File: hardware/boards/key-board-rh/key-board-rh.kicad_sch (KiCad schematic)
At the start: 6 parts, among them J1 12-way, J2 2x12 1.27mm shrouded box head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, J3 1x10 2.54mm header pins, J4 1x10 2.54mm header pins, J5 4 wire pads

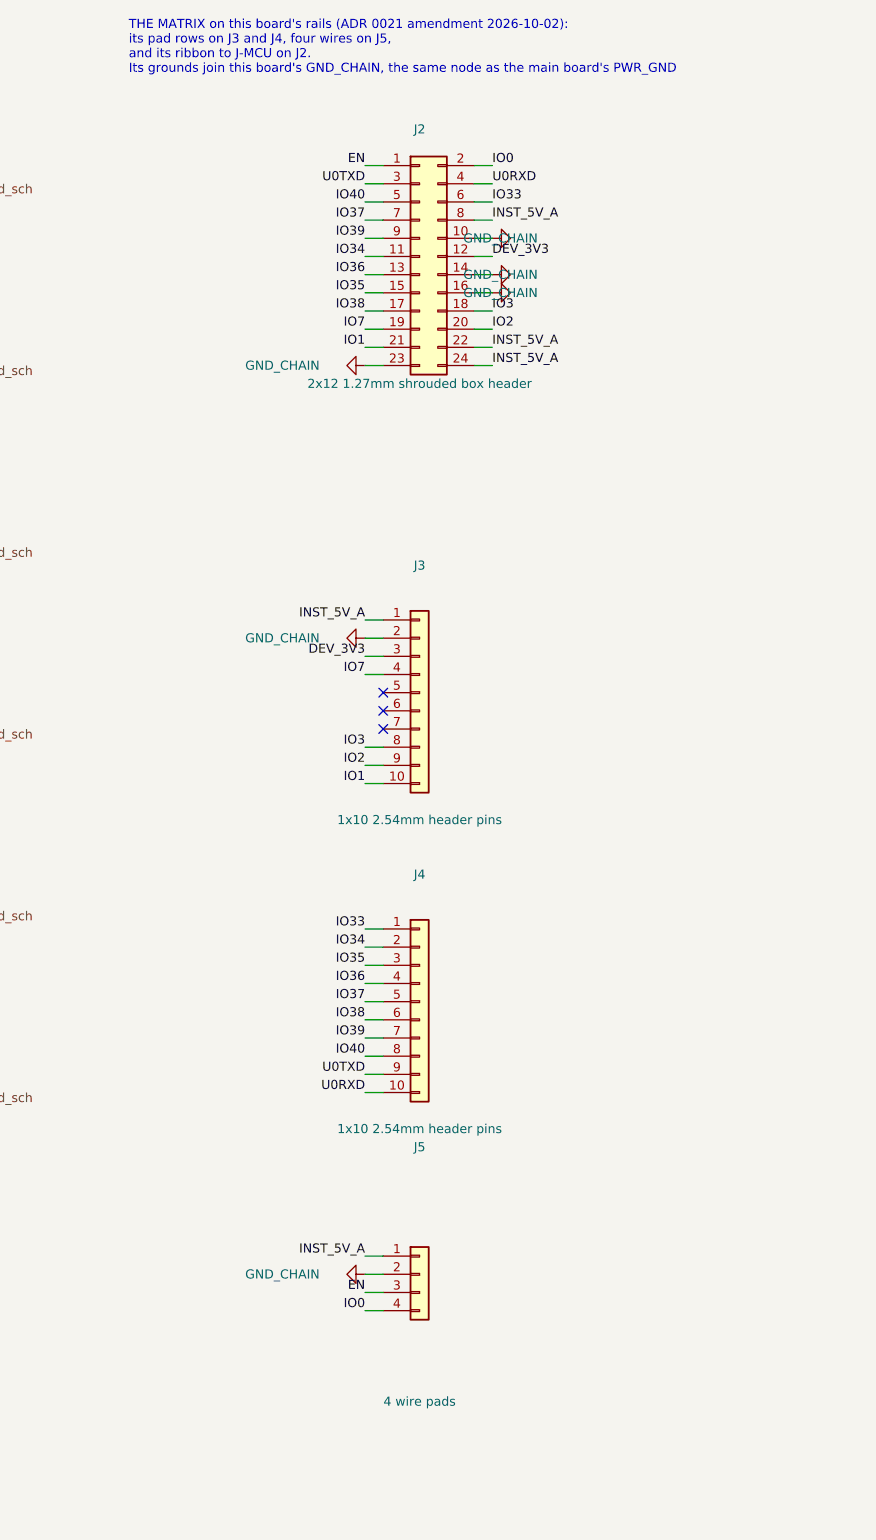
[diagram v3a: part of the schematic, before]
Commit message: WIP #23: Matrix carrier (option c) in progress - RH key board back to its original outline, EN/IO0 removed, HDR-SERVICE 1x3, carrier sheet and CAD, J-MCU at y 14.9
Checkpoint committed by the coordinator to protect uncommitted work.

Gate-Red: carrier and RH board mid-layout, CAD outputs and sims not rebuilt

Co-Authored-By: Claude Opus 5.5 <noreply@anthropic.com>
Claude-Session: https://claude.ai/code/session_01LmB4muFXnoLprWX4JzuJ5A
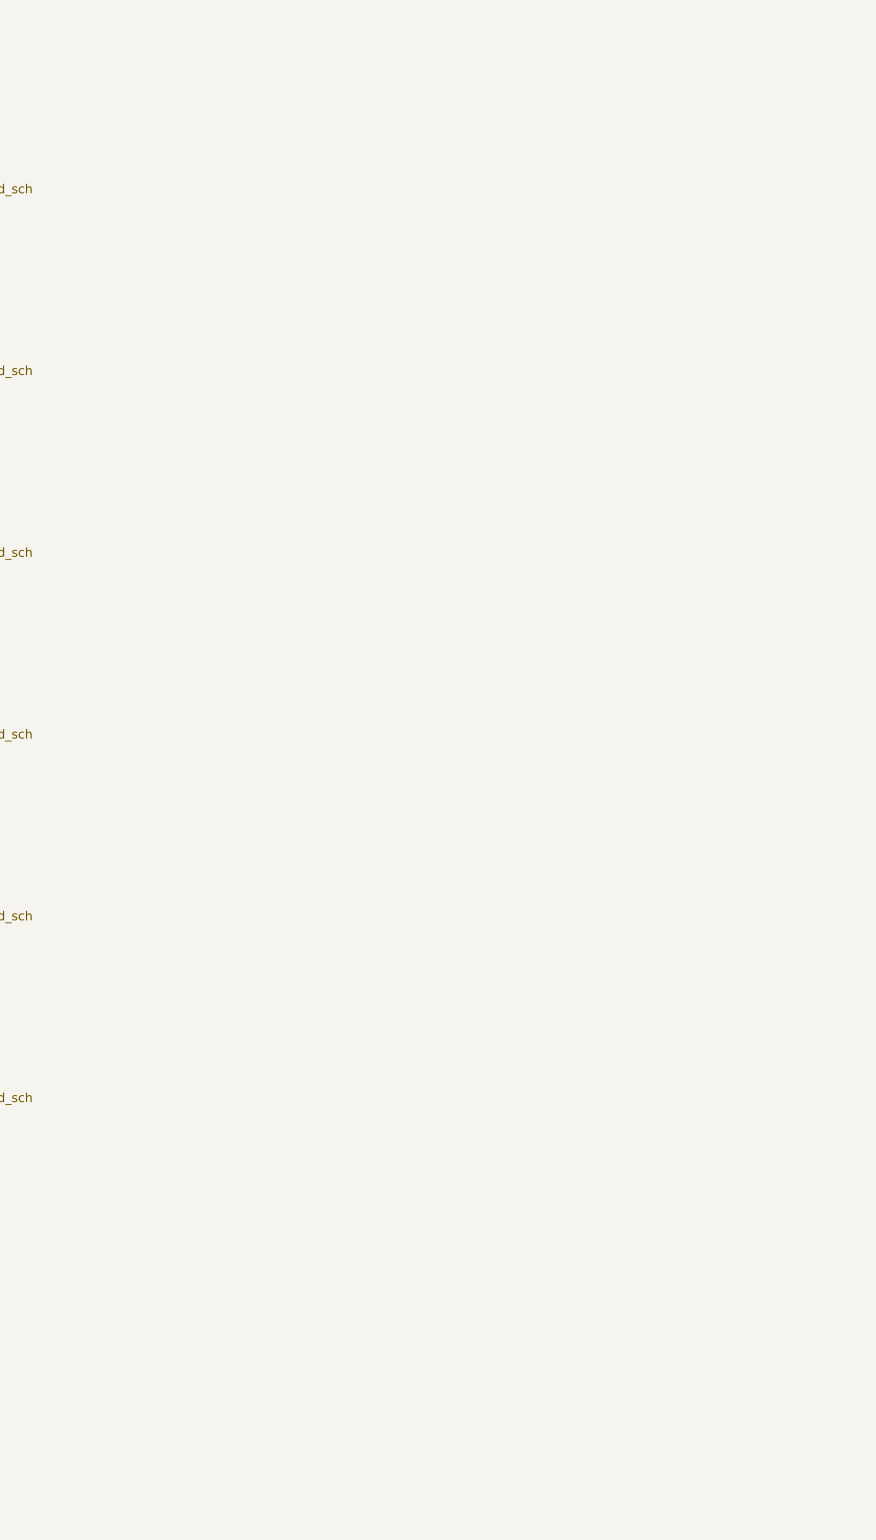
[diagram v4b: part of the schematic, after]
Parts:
- removed J2: 2x12 1.27mm shrouded box header, woody:IDC-Header_2x12_P1.27mm_XKB_X1270WR_Horizontal, symbol Connector_Generic:Conn_02x12_Odd_Even
- removed J3, J4: 1x10 2.54mm header pins, Connector_PinHeader_2.54mm:PinHeader_1x10_P2.54mm_Vertical, symbol Connector_Generic:Conn_01x10
- removed J5: 4 wire pads, Connector_PinHeader_2.54mm:PinHeader_1x04_P2.54mm_Vertical, symbol Connector_Generic:Conn_01x04
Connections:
- no-connect marks 5 -> 2
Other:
- note removed: "THE MATRIX on this board's rails (ADR 0021 amendment 2026-10-02): its pad rows on J3 and J4, four wires on J5, and its ribbon to J-MCU on J2. Its grounds join this board's GND_CHAIN, the same node as the main board's PWR_GND"
